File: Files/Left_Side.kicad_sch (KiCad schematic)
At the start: 76 parts, among them J1 USB_C_Receptacle, J3 USB_C_Receptacle, U1 W25Q128JVS, U2 XC6206-3.3_SOT, U3 USBLC6-2SC6, U4 RP2040, Y1 Crystal_GND24

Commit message: added 5v pads
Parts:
- C1, C10, C11, C12, C13, C14, C15, C16, C17, C18, C2, C3, C4, C5, C6, C7, C8, C9: footprint Capacitor_SMD:C_0805_2012Metric_Pad1.18x1.45mm_HandSolder -> Capacitor_SMD:C_0805_2012Metric
- R1, R10, R2, R3, R4, R5, R6, R7, R8, R9: footprint Resistor_SMD:R_0805_2012Metric_Pad1.20x1.40mm_HandSolder -> Resistor_SMD:R_0805_2012Metric
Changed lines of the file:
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@@
 			)
 		)
-		(property "Footprint" "Capacitor_SMD:C_0805_2012Metric_Pad1.18x1.45mm_HandSolder"
+		(property "Footprint" "Capacitor_SMD:C_0805_2012Metric"
 			(at 153.67 133.0452 0)
 			(effects
@@
 			)
 		)
-		(property "Footprint" "Resistor_SMD:R_0805_2012Metric_Pad1.20x1.40mm_HandSolder"
+		(property "Footprint" "Resistor_SMD:R_0805_2012Metric"
 			(at 87.63 185.928 90)
 			(effects
@@
 			)
 		)
-		(property "Footprint" "Capacitor_SMD:C_0805_2012Metric_Pad1.18x1.45mm_HandSolder"
+		(property "Footprint" "Capacitor_SMD:C_0805_2012Metric"
 			(at 138.1252 186.69 0)
 			(effects
@@
 			)
 		)
-		(property "Footprint" "Capacitor_SMD:C_0805_2012Metric_Pad1.18x1.45mm_HandSolder"
+		(property "Footprint" "Capacitor_SMD:C_0805_2012Metric"
 			(at 84.1248 57.15 0)
 			(effects
@@
 			)
 		)
-		(property "Footprint" "Resistor_SMD:R_0805_2012Metric_Pad1.20x1.40mm_HandSolder"
+		(property "Footprint" "Resistor_SMD:R_0805_2012Metric"
 			(at 185.42 144.018 90)
 			(effects
@@
 			)
 		)
-		(property "Footprint" "Capacitor_SMD:C_0805_2012Metric_Pad1.18x1.45mm_HandSolder"
+		(property "Footprint" "Capacitor_SMD:C_0805_2012Metric"
 			(at 186.3852 76.2 0)
 			(effects
@@
 			)
 		)
-		(property "Footprint" "Capacitor_SMD:C_0805_2012Metric_Pad1.18x1.45mm_HandSolder"
+		(property "Footprint" "Capacitor_SMD:C_0805_2012Metric"
 			(at 279.0952 60.96 0)
 			(effects
@@
 			)
 		)
-		(property "Footprint" "Capacitor_SMD:C_0805_2012Metric_Pad1.18x1.45mm_HandSolder"
+		(property "Footprint" "Capacitor_SMD:C_0805_2012Metric"
 			(at 186.3852 60.96 0)
 			(effects
@@
 			)
 		)
-		(property "Footprint" "Resistor_SMD:R_0805_2012Metric_Pad1.20x1.40mm_HandSolder"
+		(property "Footprint" "Resistor_SMD:R_0805_2012Metric"
 			(at 185.42 95.758 90)
 			(effects
@@
 			)
 		)
-		(property "Footprint" "Capacitor_SMD:C_0805_2012Metric_Pad1.18x1.45mm_HandSolder"
+		(property "Footprint" "Capacitor_SMD:C_0805_2012Metric"
 			(at 121.92 105.7148 0)
 			(effects
@@
 			)
 		)
-		(property "Footprint" "Capacitor_SMD:C_0805_2012Metric_Pad1.18x1.45mm_HandSolder"
+		(property "Footprint" "Capacitor_SMD:C_0805_2012Metric"
 			(at 153.67 143.2052 0)
 			(effects
@@
 			)
 		)
-		(property "Footprint" "Capacitor_SMD:C_0805_2012Metric_Pad1.18x1.45mm_HandSolder"
+		(property "Footprint" "Capacitor_SMD:C_0805_2012Metric"
 			(at 318.4652 60.96 0)
 			(effects
@@
 			)
 		)
-		(property "Footprint" "Capacitor_SMD:C_0805_2012Metric_Pad1.18x1.45mm_HandSolder"
+		(property "Footprint" "Capacitor_SMD:C_0805_2012Metric"
 			(at 105.1052 186.69 0)
 			(effects
@@
 			)
 		)
-		(property "Footprint" "Capacitor_SMD:C_0805_2012Metric_Pad1.18x1.45mm_HandSolder"
+		(property "Footprint" "Capacitor_SMD:C_0805_2012Metric"
 			(at 304.4952 60.96 0)
 			(effects
@@
 			)
 		)
-		(property "Footprint" "Capacitor_SMD:C_0805_2012Metric_Pad1.18x1.45mm_HandSolder"
+		(property "Footprint" "Capacitor_SMD:C_0805_2012Metric"
 			(at 267.6652 60.96 0)
 			(effects
@@
 			)
 		)
-		(property "Footprint" "Capacitor_SMD:C_0805_2012Metric_Pad1.18x1.45mm_HandSolder"
+		(property "Footprint" "Capacitor_SMD:C_0805_2012Metric"
 			(at 254.9652 60.96 0)
 			(effects
@@
 			)
 		)
-		(property "Footprint" "Capacitor_SMD:C_0805_2012Metric_Pad1.18x1.45mm_HandSolder"
+		(property "Footprint" "Capacitor_SMD:C_0805_2012Metric"
 			(at 197.8152 60.96 0)
 			(effects
@@
 			)
 		)
-		(property "Footprint" "Capacitor_SMD:C_0805_2012Metric_Pad1.18x1.45mm_HandSolder"
+		(property "Footprint" "Capacitor_SMD:C_0805_2012Metric"
 			(at 242.2652 76.2 0)
 			(effects
@@
 			)
 		)
-		(property "Footprint" "Capacitor_SMD:C_0805_2012Metric_Pad1.18x1.45mm_HandSolder"
+		(property "Footprint" "Capacitor_SMD:C_0805_2012Metric"
 			(at 240.9952 41.91 0)
 			(effects
@@
 			)
 		)
-		(property "Footprint" "Resistor_SMD:R_0805_2012Metric_Pad1.20x1.40mm_HandSolder"
+		(property "Footprint" "Resistor_SMD:R_0805_2012Metric"
 			(at 185.42 94.742 90)
 			(effects
@@
 			)
 		)
-		(property "Footprint" "Resistor_SMD:R_0805_2012Metric_Pad1.20x1.40mm_HandSolder"
+		(property "Footprint" "Resistor_SMD:R_0805_2012Metric"
 			(at 87.63 188.468 90)
 			(effects
@@
 			)
 		)
-		(property "Footprint" "Resistor_SMD:R_0805_2012Metric_Pad1.20x1.40mm_HandSolder"
+		(property "Footprint" "Resistor_SMD:R_0805_2012Metric"
 			(at 95.758 110.49 90)
 			(effects
@@
 			)
 		)
-		(property "Footprint" "Capacitor_SMD:C_0805_2012Metric_Pad1.18x1.45mm_HandSolder"
+		(property "Footprint" "Capacitor_SMD:C_0805_2012Metric"
 			(at 291.7952 60.96 0)
 			(effects
@@
 			)
 		)
-		(property "Footprint" "Resistor_SMD:R_0805_2012Metric_Pad1.20x1.40mm_HandSolder"
+		(property "Footprint" "Resistor_SMD:R_0805_2012Metric"
 			(at 211.582 208.28 90)
 			(effects
@@
 			)
 		)
-		(property "Footprint" "Capacitor_SMD:C_0805_2012Metric_Pad1.18x1.45mm_HandSolder"
+		(property "Footprint" "Capacitor_SMD:C_0805_2012Metric"
 			(at 242.2652 60.96 0)
 			(effects
@@
 			)
 		)
-		(property "Footprint" "Resistor_SMD:R_0805_2012Metric_Pad1.20x1.40mm_HandSolder"
+		(property "Footprint" "Resistor_SMD:R_0805_2012Metric"
 			(at 76.962 50.8 90)
 			(effects
@@
 			)
 		)
-		(property "Footprint" "Resistor_SMD:R_0805_2012Metric_Pad1.20x1.40mm_HandSolder"
+		(property "Footprint" "Resistor_SMD:R_0805_2012Metric"
 			(at 85.09 113.538 90)
 			(effects
@@
 			)
 		)
-		(property "Footprint" "Resistor_SMD:R_0805_2012Metric_Pad1.20x1.40mm_HandSolder"
+		(property "Footprint" "Resistor_SMD:R_0805_2012Metric"
 			(at 181.102 208.28 90)
 			(effects

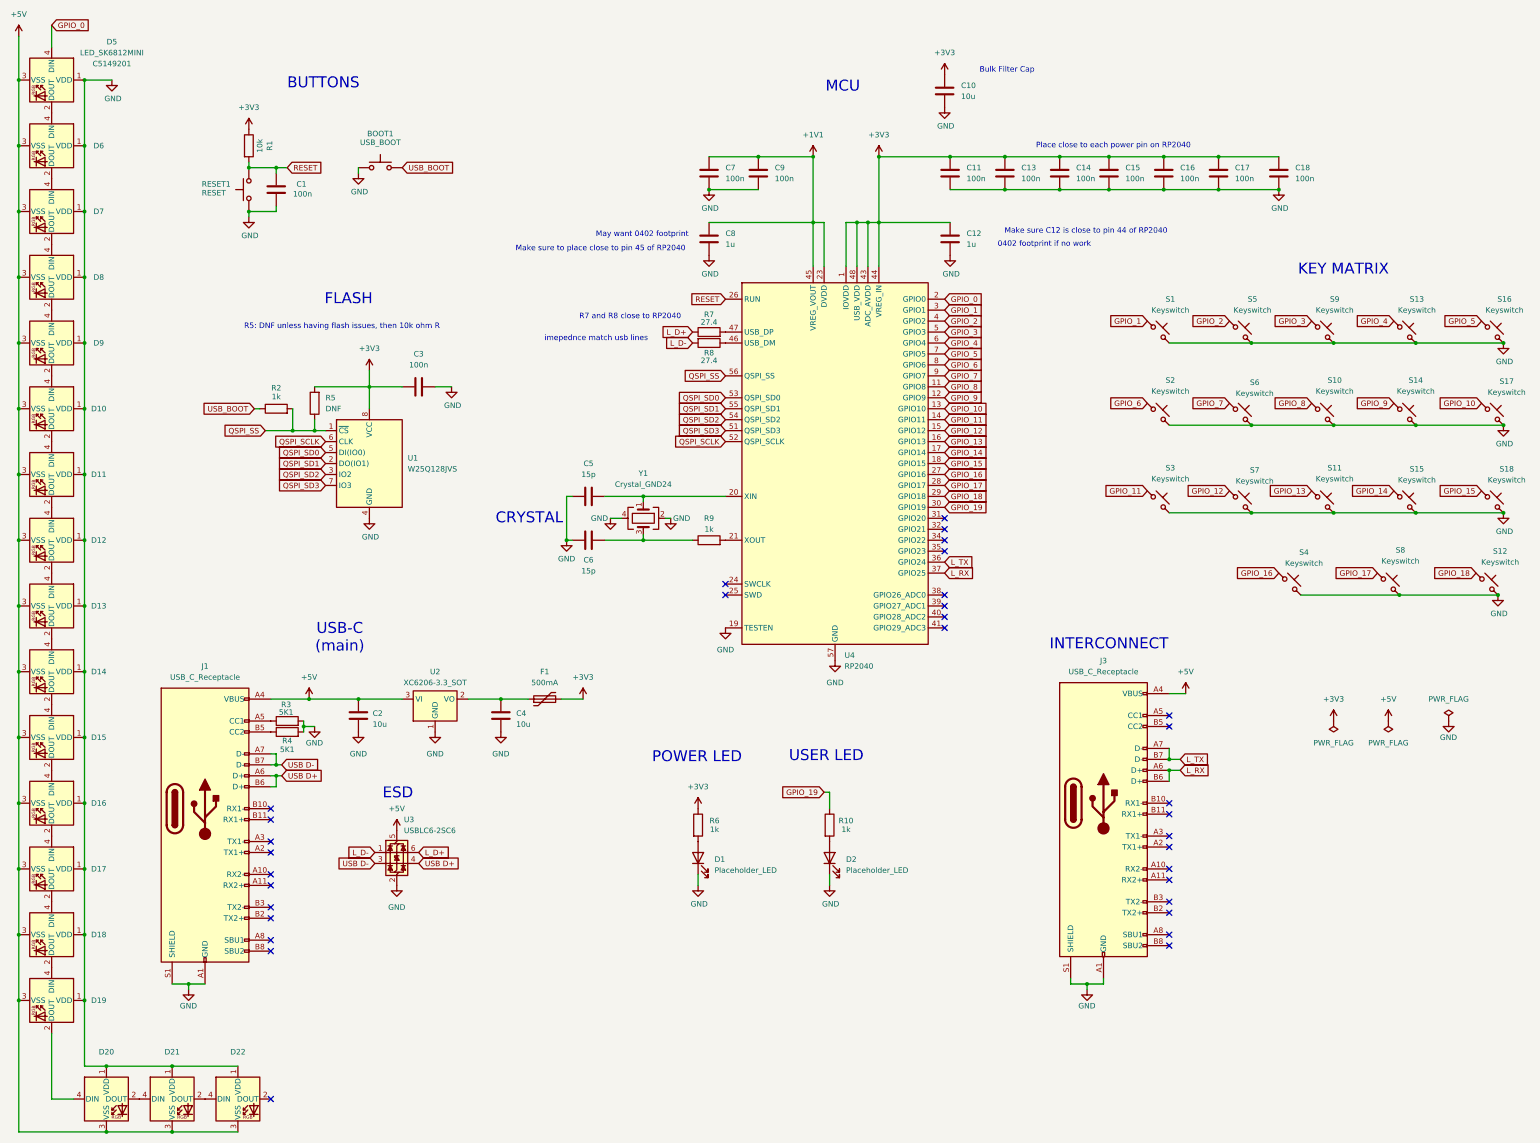
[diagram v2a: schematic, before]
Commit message: converted to 4 layer board
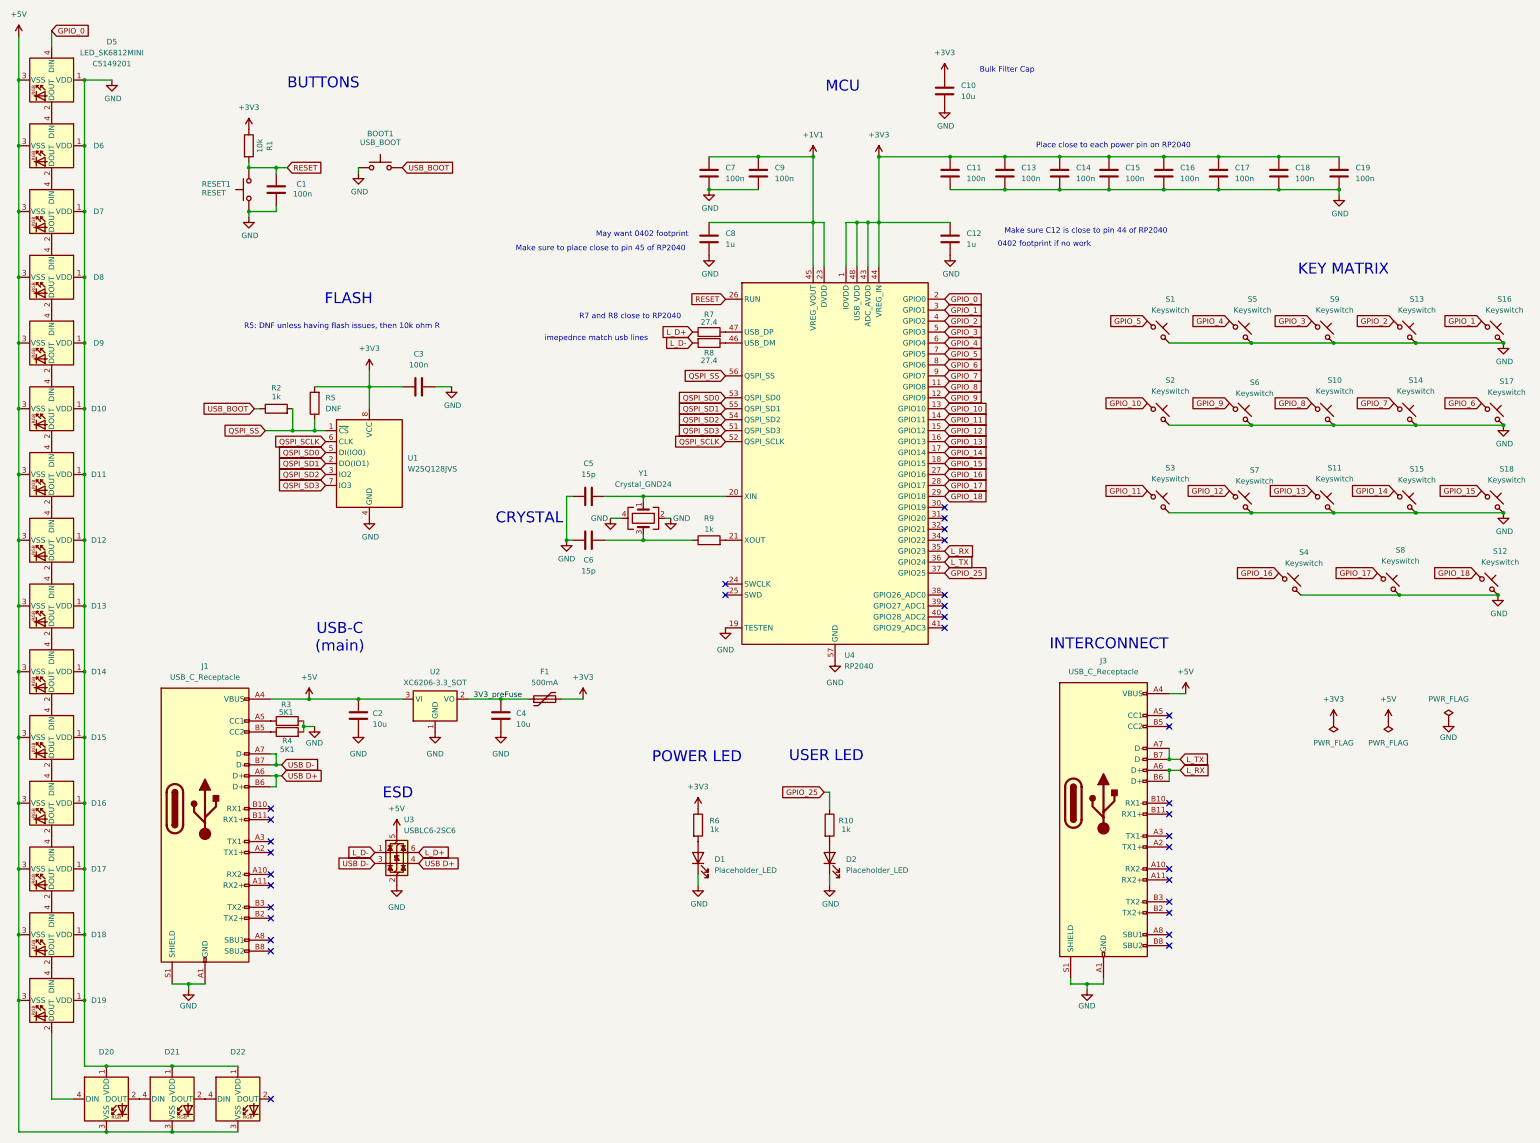
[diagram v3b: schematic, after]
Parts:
- added C19: 100n, Capacitor_SMD:C_0603_1608Metric, symbol Device:C
- C1, C10, C11, C12, C13, C14, C15, C16, C17, C18, C2, C3, C4, C5, C6, C7, C8, C9: footprint Capacitor_SMD:C_0805_2012Metric -> Capacitor_SMD:C_0603_1608Metric
- R1, R10, R2, R3, R4, R5, R6, R7, R8, R9: footprint Resistor_SMD:R_0805_2012Metric -> Resistor_SMD:R_0603_1608Metric
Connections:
- net +3V3: now also C19.1
- net GND: now also C19.2
- net GPIO_1: now also S16.1; no longer S1.1
- net GPIO_10: now also S2.1; no longer S17.1
- net GPIO_2: now also S13.1; no longer S5.1
- net GPIO_4: now also S5.1; no longer S13.1
- net GPIO_5: now also S1.1; no longer S16.1
- net GPIO_6: now also S17.1; no longer S2.1
- net GPIO_7: now also S14.1; no longer S6.1
- net GPIO_9: now also S6.1; no longer S14.1
- net L_RX: now also U4.35 (GPIO23); no longer U4.37 (GPIO25)
- net 3V3_preFuse: now reaches C4.1, F1.1, U2.2 (VO)
- net GPIO_19: no longer names the net of U4.30 (GPIO19)
- net GPIO_19: no longer R10.1
- new net GPIO_25: R10.1, U4.37 (GPIO25)
